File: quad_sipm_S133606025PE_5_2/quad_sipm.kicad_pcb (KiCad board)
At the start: 2 copper layers, 100 x 100 mm, 21 parts, among them J1 8-102202-4, J2 8-102202-4, J3 8-102202-4, J4 8-102202-4

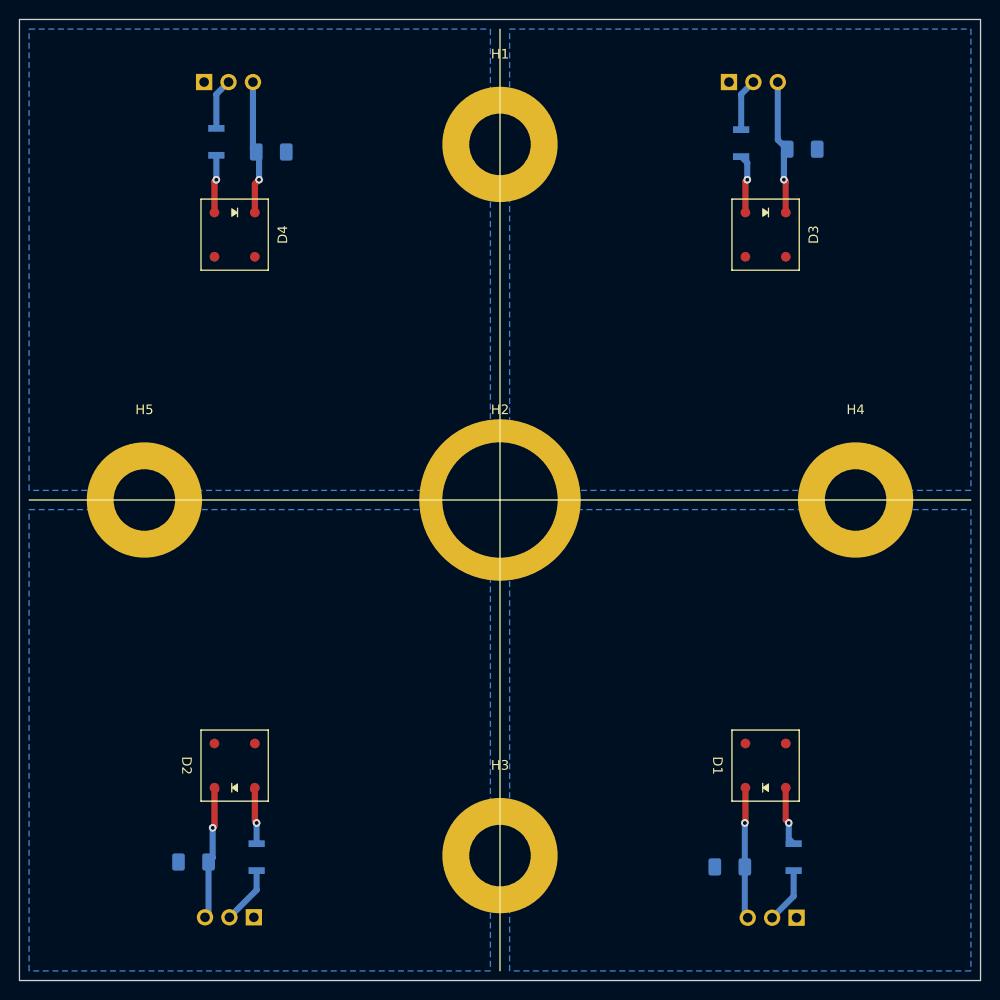
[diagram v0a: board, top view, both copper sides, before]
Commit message: added Rev 8.1: attenuator switch
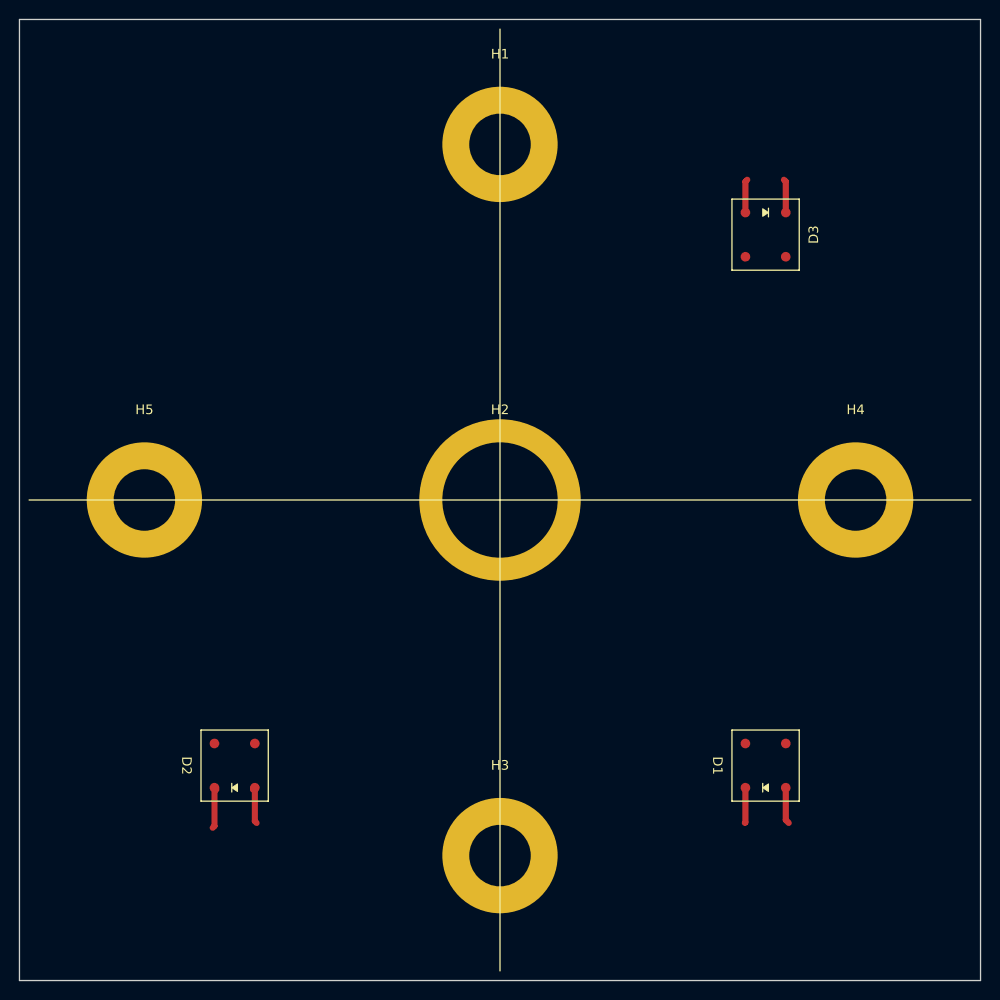
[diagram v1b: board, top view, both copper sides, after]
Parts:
- removed C1, C2, C3, C4: 10nF 100V, Capacitor_SMD:C_1206_3216Metric_Pad1.33x1.80mm_HandSolder
- removed D4: 1N914, Diode_SMD:S13360-6025PE
- removed J1, J2, J3, J4: 8-102202-4, Connector_PinHeader_2.54mm:PinHeader_1x03_P2.54mm_Vertical
- removed R1, R2, R3, R4: R, Resistor_SMD:1206_VIS-L
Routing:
- net Net-(D4-K): track 13.6 -> 0.00 mm, vias 1 -> 0
- net Net-(D3-K): track 14.2 -> 3.50 mm, vias 1 -> 0
- net Net-(D1-K): track 13.7 -> 3.69 mm, vias 1 -> 0
- net Net-(D2-K): track 14.2 -> 4.53 mm, vias 1 -> 0
- net Net-(D4-A): track 6.04 -> 0.00 mm, vias 1 -> 0
- net Net-(J2-Pin_2): track 6.03 -> 0.00 mm
- net Net-(J1-Pin_2): track 5.83 -> 0.00 mm
- net Net-(J3-Pin_2): track 5.48 -> 0.00 mm
- net Net-(J4-Pin_2): track 5.34 -> 0.00 mm
- net Net-(D3-A): track 6.17 -> 3.50 mm, vias 1 -> 0
- net Net-(D1-A): track 6.16 -> 3.80 mm, vias 1 -> 0
- net Net-(D2-A): track 6.18 -> 4.02 mm, vias 1 -> 0
- removed copper zone on B.Cu, net Net-(J1-Pin_1)
- removed copper zone on B.Cu, net Net-(J2-Pin_1)
- removed copper zone on B.Cu, net Net-(J3-Pin_1)
- removed copper zone on B.Cu, net Net-(J4-Pin_1)
